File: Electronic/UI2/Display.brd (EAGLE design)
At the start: 160 x 100 mm, 6 parts, among them Q1 2N3906

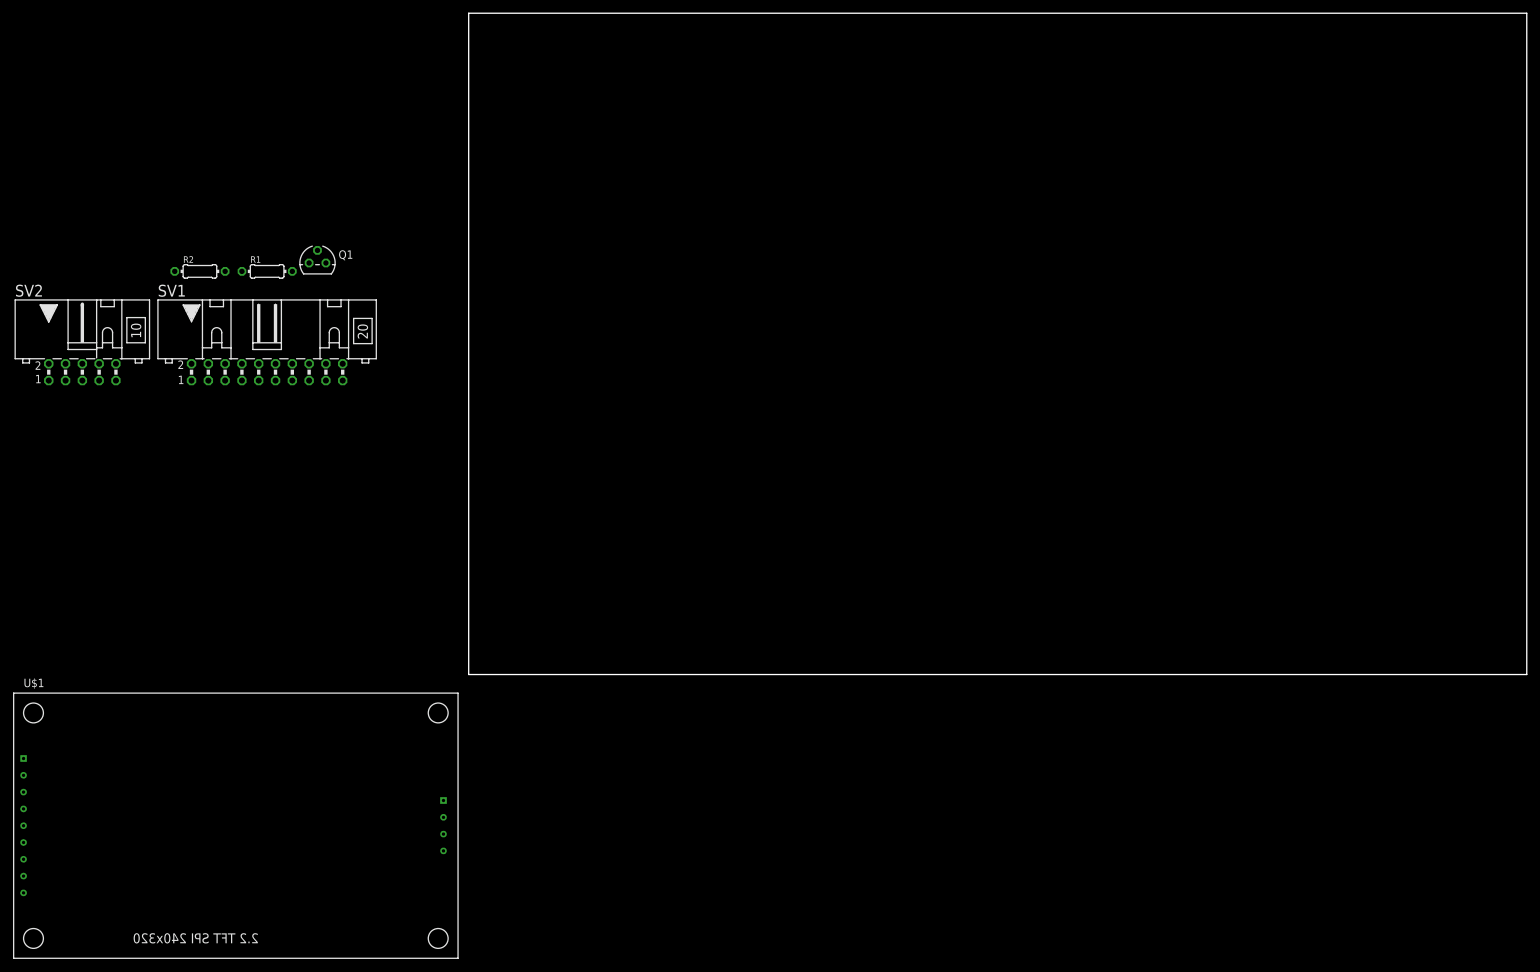
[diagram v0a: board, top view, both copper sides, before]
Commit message: new Keycross and EC60A board
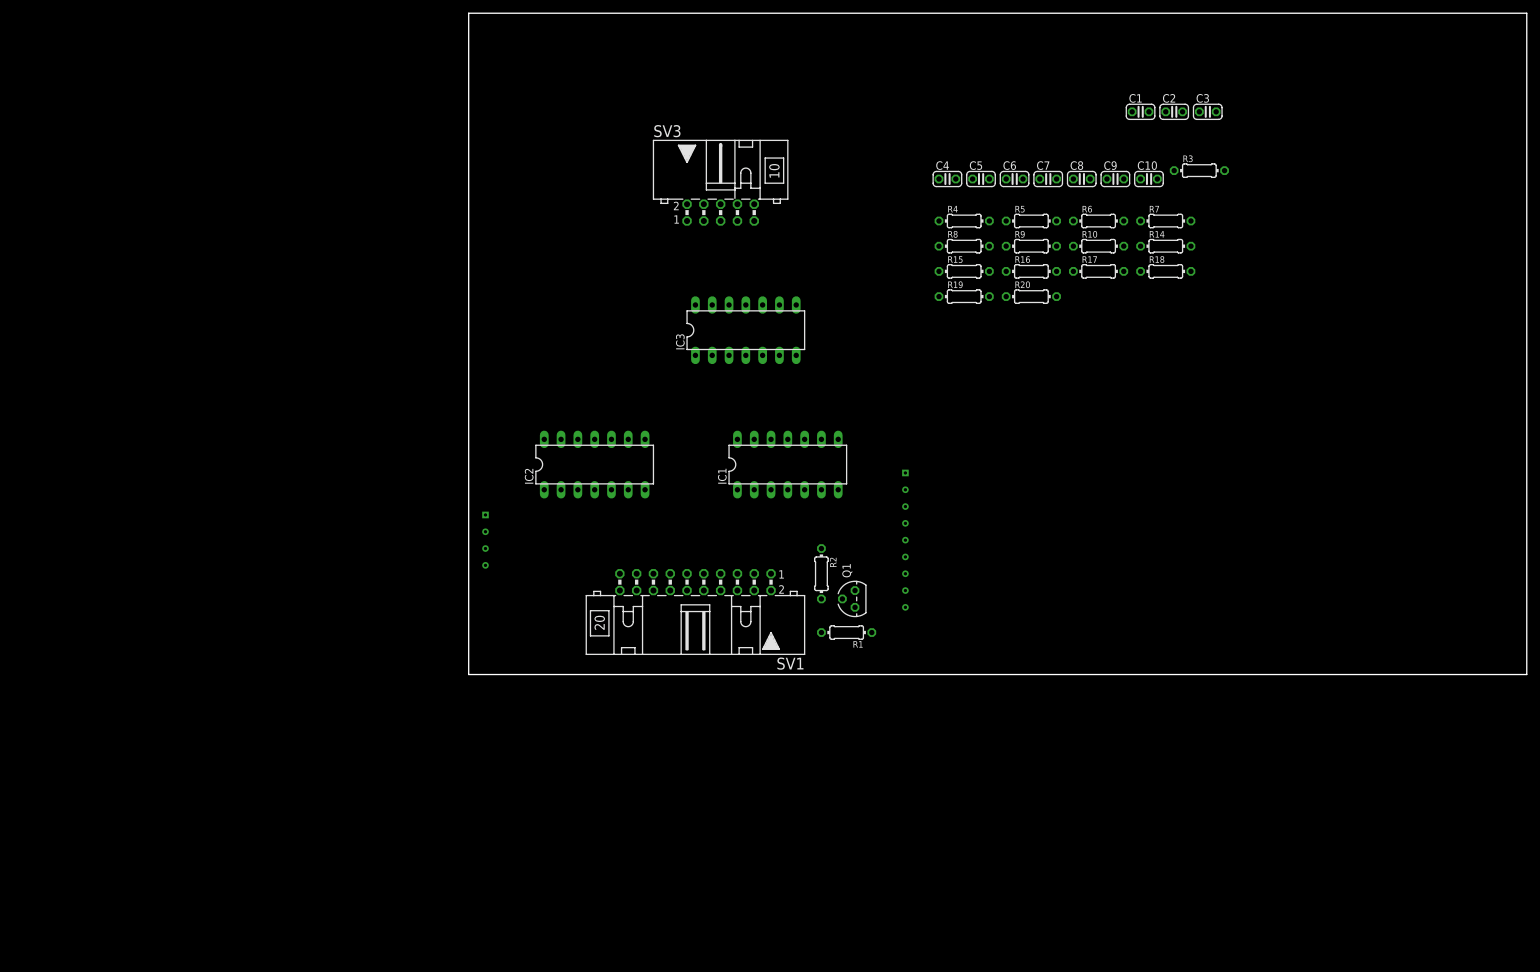
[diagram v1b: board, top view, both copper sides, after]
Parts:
- removed SV2: KEY_PAD, con-harting-ml:ML10L
- added C1, C10, C2, C3, C4, C5, C6, C7, C8, C9: .1µ, rcl:C025-024X044
- added IC1, IC2: 74HCT14N, 74xx-eu:DIL14
- added IC3: 74HCT74N, 74xx-eu:DIL14
- added R10, R15, R4, R6, R8: 82k, resistor:0204/7
- added R14, R3, R5, R7, R9: 15k, resistor:0204/7
- added R16, R17, R18, R19: 10k, resistor:0204/7
- added R20: 3k3, resistor:0204/7
- added SV3: (no value), con-harting-ml:ML10L
- moved U$1 140.2 mm to (66.0, 30.5), flipped to the bottom
- moved R2 104.5 mm to (53.3, 15.2), turned to 270 degrees
- moved R1 103.3 mm to (57.1, 6.35), turned to 180 degrees
- moved Q1 95.8 mm to (58.4, 11.4), turned to 90 degrees
- moved SV1 72.1 mm to (34.3, 14.0), turned to 180 degrees
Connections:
- removed net ENC-DIR: SV2.5
- removed net ENC-STEP: SV2.7
- new net ENC1: C5.1, IC2.11, R16.2
- new net ENC2: C6.1, IC2.13, R17.2
- new net ENC_1: R16.1, R18.1, SV3.7
- new net ENC_2: R17.1, R19.2, SV3.5
- new net K1: C9.1, IC1.13, R14.2
- new net K2: C1.1, IC1.11, R3.2
- new net K3: C2.1, IC1.9, R5.2
- new net K4: C3.1, IC1.3, R7.2
- new net K5: C4.1, IC1.1, R9.2
- new net K_1: R14.1, R15.1, SV3.4
- new net K_2: R3.1, R4.1, SV3.6
- new net K_3: R5.1, R6.1, SV3.8
- new net K_4: R10.1, R9.1, SV3.10
- new net K_5: R7.1, R8.1, SV3.9
- new net N$1: IC2.10, IC3.2
- new net N$3: IC3.1, IC3.4, R20.2
- net !MEM_CS: now also U$1.SD_CS
- net +3.3V: now also C10.1, C7.1, C8.1, IC1.14, IC2.14, IC3.14, R10.2, R15.2, R18.2, R19.1, R20.1, R4.2, R6.2, R8.2, SV3.1; no longer SV2.1
- net ENC_DIR: now also IC3.5
- net ENC_STEP: now also IC2.12, IC3.3
- net GND: now also C1.2, C10.2, C2.2, C3.2, C4.2, C5.2, C6.2, C7.2, C8.2, C9.2, IC1.7, IC2.7, IC3.7, SV3.2; no longer SV2.2
- net KEY_1: now also IC1.12; no longer SV2.4
- net KEY_2: now also IC1.10; no longer SV2.6
- net KEY_3: now also IC1.8; no longer SV2.8
- net KEY_4: now also IC1.2; no longer SV2.10
- net KEY_5: now also IC1.4; no longer SV2.9
- net MISO: now also U$1.SD_MISO
- net MOSI: now also U$1.SD_MOSI
- net SCLK: now also U$1.SD_SCK
